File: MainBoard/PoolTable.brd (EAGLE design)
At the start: 457.2 x 166 mm, 85 parts, among them IC1 LM317MBSTT3, IC2 LM317MBSTT3, IC3 LM317MBSTT3, IC5 MIC2026-1YM, IC7 AP2331W-7, J1 USB_A_SMT_FEMALE, J2 USB_A_SMT_FEMALE, J4 SD_CARD_SOCKET, Q1 DMG1012T-7, Q2 DMG1012T-7, Q3 DMG1012T-7, U1 TMP102, U2 TMP102, U3 TMP102, U4 TMP102, U5 LAN9512-JZX, U6 FSUSB42UMX

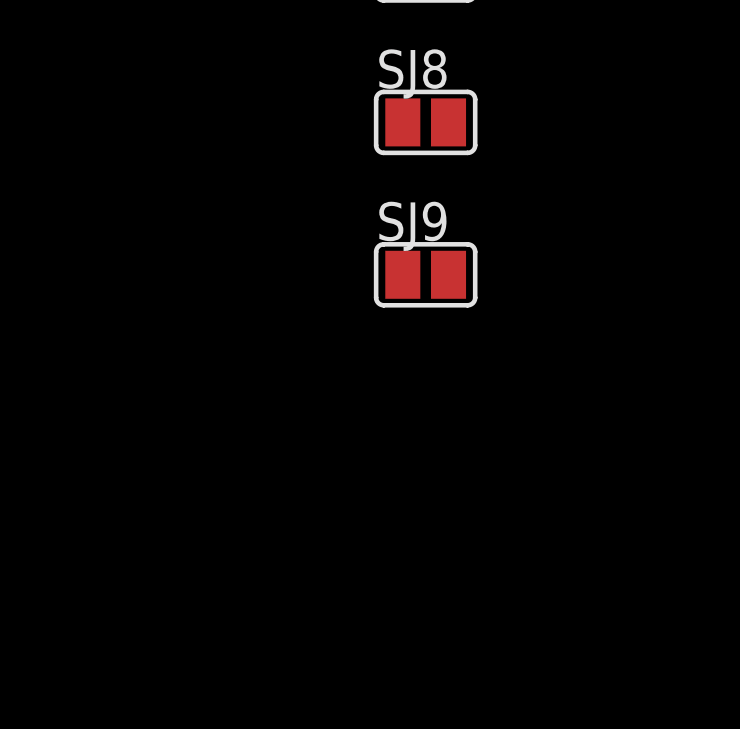
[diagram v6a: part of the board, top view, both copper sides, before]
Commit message: Added EEPROM for LAN9512
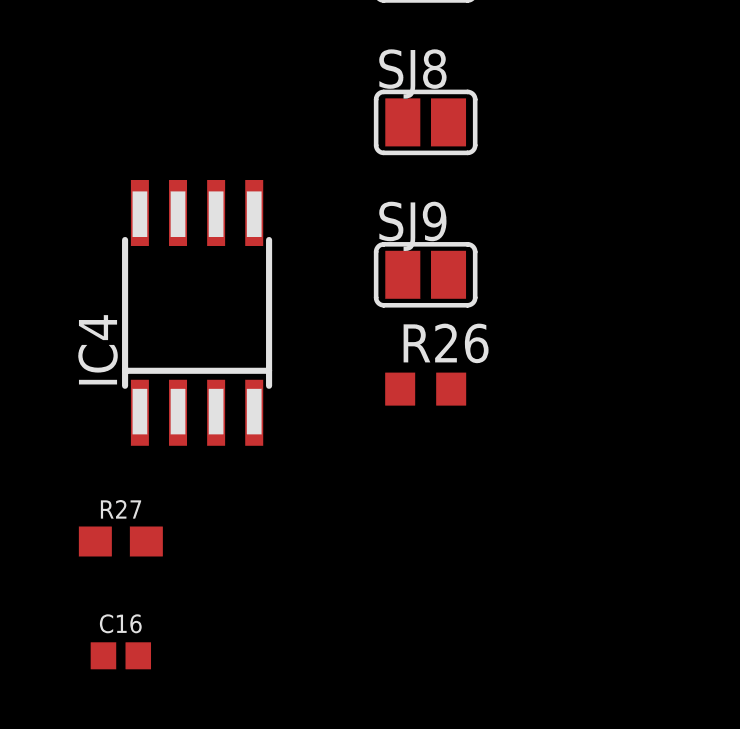
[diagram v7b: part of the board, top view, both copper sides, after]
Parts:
- added C16: 0.1uF, SparkFun-Capacitors:0402
- added IC4: 93LC66SM, microchip:SO-08M
- added R26: 12.4K, adafruit:R0603
- added R27: 10k, SparkFun-Resistors:0603
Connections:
- new net CPU1_ETH_EECLK: IC4.2, U5.23
- new net CPU1_ETH_EECS: IC4.1, R27.1, U5.24
- new net CPU1_ETH_EEDI: IC4.4, U5.26
- new net CPU1_ETH_EEDO: IC4.3, U5.25
- new net N$4: R26.2, U5.50
- new net NRESET: U5.12
- net 3.3V: now also C16.1, IC4.8
- net GND: now also C16.2, IC4.5, R26.1, R27.2
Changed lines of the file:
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@@
 <?xml version="1.0" encoding="utf-8"?>
 <!DOCTYPE eagle SYSTEM "eagle.dtd">
-<eagle version="9.3.0">
+<eagle version="9.2.2">
 <drawing>
 <settings>
@@
 <attribute name="VALUE" x="-59.2899" y="-494.03" size="0.02" layer="27"/>
 </element>
+<element name="R26" library="adafruit" package="R0603" value="12.4K" x="-59.69" y="-497.84" smashed="yes">
+<attribute name="NAME" x="-60.579" y="-496.951" size="1.27" layer="25"/>
+<attribute name="VALUE" x="-60.579" y="-499.872" size="1.27" layer="27"/>
+</element>
+<element name="IC4" library="microchip" library_urn="urn:adsk.eagle:library:294" package="SO-08M" package3d_urn="urn:adsk.eagle:package:20798/1" value="93LC66SM" x="-67.31" y="-495.3" smashed="yes">
+<attribute name="MF" value="MICROCHIP" x="-67.31" y="-495.3" size="1.778" layer="27" display="off"/>
+<attribute name="MPN" value="93LC66/SN" x="-67.31" y="-495.3" size="1.778" layer="27" display="off"/>
+<attribute name="NAME" x="-69.977" y="-497.84" size="1.27" layer="25" rot="R90"/>
+<attribute name="OC_FARNELL" value="1296586" x="-67.31" y="-495.3" size="1.778" layer="27" display="off"/>
+<attribute name="OC_NEWARK" value="65K1154" x="-67.31" y="-495.3" size="1.778" layer="27" display="off"/>
+<attribute name="VALUE" x="-63.373" y="-497.84" size="1.27" layer="27" rot="R90"/>
+</element>
+<element name="R27" library="SparkFun-Resistors" package="0603" value="10k" x="-69.85" y="-502.92" smashed="yes">
+<attribute name="NAME" x="-69.85" y="-502.158" size="0.6096" layer="25" font="vector" ratio="20" align="bottom-center"/>
+<attribute name="PROD_ID" value="RES-00824" x="-69.85" y="-502.92" size="1.778" layer="27" display="off"/>
+<attribute name="VALUE" x="-69.85" y="-503.682" size="0.6096" layer="27" font="vector" ratio="20" align="top-center"/>
+</element>
+<element name="C16" library="SparkFun-Capacitors" package="0402" value="0.1uF" x="-69.85" y="-506.73" smashed="yes">
+<attribute name="NAME" x="-69.85" y="-505.968" size="0.6096" layer="25" font="vector" ratio="20" align="bottom-center"/>
+<attribute name="PROD_ID" value="CAP-12416" x="-69.85" y="-506.73" size="1.778" layer="27" display="off"/>
+<attribute name="VALUE" x="-69.85" y="-507.492" size="0.6096" layer="27" font="vector" ratio="20" align="top-center"/>
+</element>
 </elements>
 <signals>
@@
 <contactref element="CAM0" pad="23"/>
 <contactref element="CAM0" pad="24"/>
+<contactref element="R26" pad="1"/>
+<contactref element="IC4" pad="5"/>
+<contactref element="R27" pad="2"/>
+<contactref element="C16" pad="2"/>
 <wire x1="-55.82" y1="-448.8" x2="-57.32" y2="-448.8" width="0" layer="19" extent="1-1"/>
 <wire x1="-54.32" y1="-448.8" x2="-55.82" y2="-448.8" width="0" layer="19" extent="1-1"/>
@@
 <wire x1="19.05" y1="-217.17" x2="19.05" y2="-247.65" width="0" layer="19" extent="1-1"/>
 <wire x1="19.05" y1="-186.69" x2="19.05" y2="-217.17" width="0" layer="19" extent="1-1"/>
+<wire x1="-65.405" y1="-491.97" x2="-59.595" y2="-450.7" width="0" layer="19" extent="1-1"/>
+<wire x1="-60.54" y1="-497.84" x2="-65.405" y2="-491.97" width="0" layer="19" extent="1-1"/>
+<wire x1="-69" y1="-502.92" x2="-60.54" y2="-497.84" width="0" layer="19" extent="1-1"/>
+<wire x1="-69.27" y1="-506.73" x2="-69" y2="-502.92" width="0" layer="19" extent="1-1"/>
 <wire x1="-9.69" y1="-144.776696875" x2="19.05" y2="-186.69" width="0" layer="19" extent="1-1"/>
 <wire x1="-9.69" y1="-137.156696875" x2="-9.69" y2="-144.776696875" width="0" layer="19" extent="1-1"/>
@@
 <contactref element="CAM1" pad="22"/>
 <contactref element="CAM0" pad="22"/>
+<contactref element="IC4" pad="8"/>
+<contactref element="C16" pad="1"/>
 <wire x1="-46.82" y1="-439.91" x2="-46.82" y2="-448.8" width="0" layer="19" extent="1-1"/>
 <wire x1="-58.928" y1="-416.56" x2="-46.82" y2="-439.91" width="0" layer="19" extent="1-1"/>
@@
 <wire x1="-48.95" y1="-318.77" x2="-56.3" y2="-330.2" width="0" layer="19" extent="1-1"/>
 <wire x1="-49.53" y1="-312.9215" x2="-48.95" y2="-318.77" width="0" layer="19" extent="1-1"/>
+<wire x1="-69.215" y1="-491.97" x2="-46.82" y2="-448.8" width="0" layer="19" extent="1-1"/>
+<wire x1="-70.43" y1="-506.73" x2="-69.215" y2="-491.97" width="0" layer="19" extent="1-1"/>
 <wire x1="-7.83" y1="-278.7142" x2="-49.53" y2="-312.9215" width="0" layer="19" extent="1-1"/>
 <wire x1="-3.83" y1="-278.7142" x2="-7.83" y2="-278.7142" width="0" layer="19" extent="1-1"/>
@@
 <contactref element="SJ4" pad="1"/>
 </signal>
+<signal name="NRESET">
+<contactref element="U5" pad="12"/>
+</signal>
+<signal name="N$4">
+<contactref element="U5" pad="50"/>
+<contactref element="R26" pad="2"/>
+<wire x1="-1.83" y1="-269.9258" x2="-58.84" y2="-497.84" width="0" layer="19" extent="1-1"/>
+</signal>
+<signal name="CPU1_ETH_EEDO">
+<contactref element="U5" pad="25"/>
+<contactref element="IC4" pad="3"/>
+<wire x1="-4.83" y1="-278.7142" x2="-66.675" y2="-498.63" width="0" layer="19" extent="1-1"/>
+</signal>
+<signal name="CPU1_ETH_EECS">
+<contactref element="U5" pad="24"/>
+<contactref element="IC4" pad="1"/>
+<contactref element="R27" pad="1"/>
+<wire x1="-69.215" y1="-498.63" x2="-70.7" y2="-502.92" width="0" layer="19" extent="1-1"/>
+<wire x1="-5.33" y1="-278.7142" x2="-69.215" y2="-498.63" width="0" layer="19" extent="1-1"/>
+</signal>
+<signal name="CPU1_ETH_EECLK">
+<contactref element="U5" pad="23"/>
+<contactref element="IC4" pad="2"/>
+<wire x1="-5.83" y1="-278.7142" x2="-67.945" y2="-498.63" width="0" layer="19" extent="1-1"/>
+</signal>
+<signal name="CPU1_ETH_EEDI">
+<contactref element="U5" pad="26"/>
+<contactref element="IC4" pad="4"/>
+<wire x1="-4.33" y1="-278.7142" x2="-65.405" y2="-498.63" width="0" layer="19" extent="1-1"/>
+</signal>
 </signals>
